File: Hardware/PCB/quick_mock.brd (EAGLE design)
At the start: 101.6 x 99.6 mm, 58 parts, among them Q3 600mA/40V

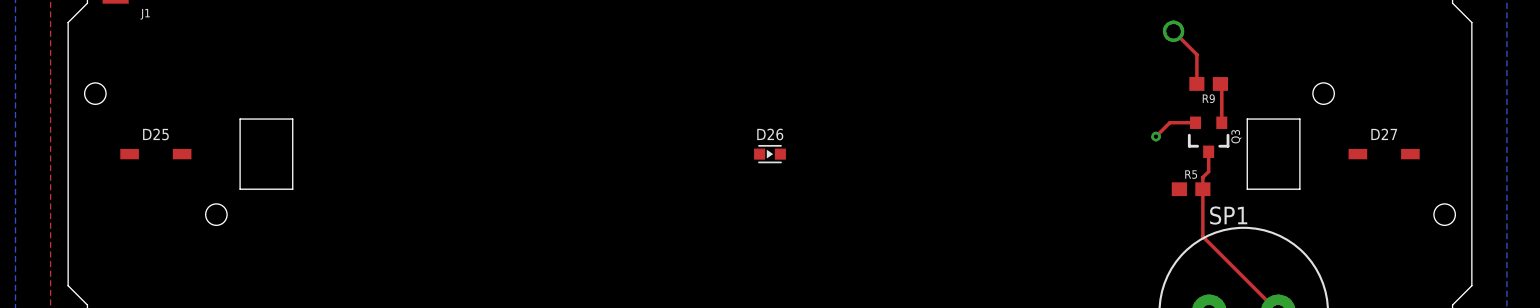
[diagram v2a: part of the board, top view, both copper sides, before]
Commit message: adjust LED placement. adjust hole and dimension placement.
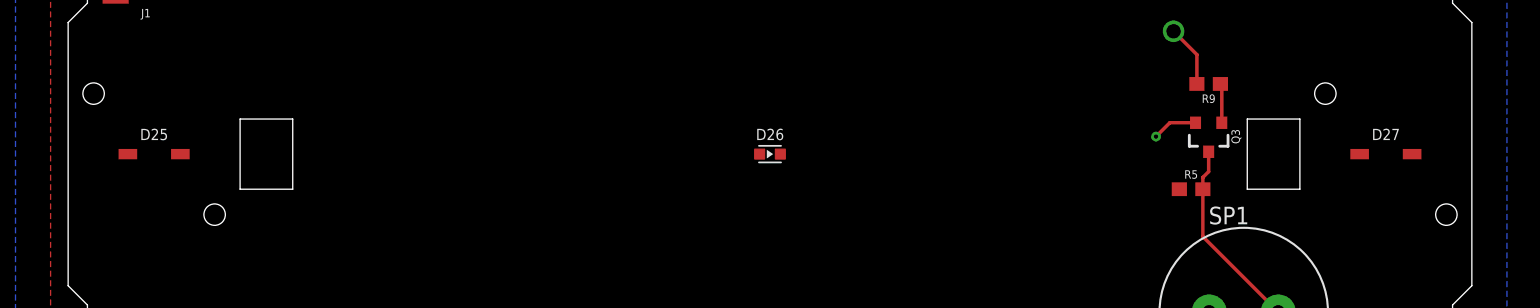
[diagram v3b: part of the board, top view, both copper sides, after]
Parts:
- moved D25 0.13 mm to (6.22, 50.8)
- moved D27 0.13 mm to (95.4, 50.8)
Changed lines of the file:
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@@
 <setting verticaltext="up"/>
 </settings>
-<grid distance="50" unitdist="mil" unit="inch" style="lines" multiple="1" display="yes" altdistance="5" altunitdist="mil" altunit="inch"/>
+<grid distance="50" unitdist="mil" unit="mm" style="lines" multiple="1" display="yes" altdistance="5" altunitdist="mil" altunit="inch"/>
 <layers>
 <layer number="1" name="Top" color="4" fill="1" visible="yes" active="yes"/>
@@
 <wire x1="13.446" y1="55.179990625" x2="13.446" y2="46.419990625" width="0.01" layer="200"/>
 <wire x1="88.17211875" y1="55.179990625" x2="88.17211875" y2="46.419990625" width="0.01" layer="200"/>
-<hole x="10.73" y="46.42" drill="1.55"/>
-<hole x="90.87" y="55.18" drill="1.55"/>
+<hole x="10.603" y="46.42" drill="1.55"/>
+<hole x="90.997" y="55.18" drill="1.55"/>
 <wire x1="90.87" y1="46.42" x2="99.63" y2="46.42" width="0.01" layer="201"/>
 <wire x1="99.63" y1="46.42" x2="99.63" y2="55.18" width="0.01" layer="201"/>
@@
 <wire x1="12.7" y1="0" x2="88.9" y2="0" width="0.01" layer="201"/>
 <wire x1="1.27" y1="88.9" x2="1.27" y2="12.7" width="0.01" layer="201"/>
-<wire x1="5.08" y1="50.8" x2="7.62" y2="50.8" width="0.1778" layer="51"/>
-<wire x1="6.35" y1="52.07" x2="6.35" y2="49.53" width="0.1778" layer="51"/>
-<wire x1="93.98" y1="50.8" x2="96.52" y2="50.8" width="0.1778" layer="51"/>
-<wire x1="95.25" y1="52.07" x2="95.25" y2="49.53" width="0.1778" layer="51"/>
+<wire x1="4.953" y1="50.8" x2="7.493" y2="50.8" width="0.1778" layer="51"/>
+<wire x1="6.223" y1="52.07" x2="6.223" y2="49.53" width="0.1778" layer="51"/>
+<wire x1="94.107" y1="50.8" x2="96.647" y2="50.8" width="0.1778" layer="51"/>
+<wire x1="95.377" y1="52.07" x2="95.377" y2="49.53" width="0.1778" layer="51"/>
 <wire x1="49.53" y1="50.8" x2="52.07" y2="50.8" width="0.1778" layer="51"/>
 <wire x1="50.8" y1="52.07" x2="50.8" y2="49.53" width="0.1778" layer="51"/>
@@
 <hole x="78.74" y="12.7" drill="2.794"/>
 <hole x="22.86" y="12.7" drill="2.794"/>
-<hole x="1.97" y="55.18" drill="1.55"/>
-<hole x="99.63" y="46.42" drill="1.55"/>
-<wire x1="7.62" y1="52.07" x2="11.43" y2="55.88" width="0.1778" layer="51"/>
-<text x="8.89" y="57.15" size="1.778" layer="51" font="vector">Transmitter</text>
+<hole x="1.843" y="55.18" drill="1.55"/>
+<hole x="99.757" y="46.42" drill="1.55"/>
+<wire x1="7.493" y1="52.07" x2="11.303" y2="55.88" width="0.1778" layer="51"/>
+<text x="8.763" y="57.15" size="1.778" layer="51" font="vector">Transmitter</text>
 <wire x1="52.07" y1="52.07" x2="55.88" y2="55.88" width="0.1778" layer="51"/>
 <text x="53.34" y="57.15" size="1.778" layer="51" font="vector">Receiver</text>
-<wire x1="96.52" y1="52.07" x2="100.33" y2="55.88" width="0.1778" layer="51"/>
-<text x="97.79" y="57.15" size="1.778" layer="51" font="vector">Transmitter</text>
+<wire x1="96.647" y1="52.07" x2="100.33" y2="55.88" width="0.1778" layer="51"/>
+<text x="97.917" y="57.15" size="1.778" layer="51" font="vector">Transmitter</text>
 <polygon width="0.1" layer="39">
 <vertex x="100.33" y="62.865"/>
@@
 <vertex x="99.06" y="37.846"/>
 </polygon>
-<circle x="99.63" y="46.42" radius="1.57" width="0" layer="39"/>
-<circle x="90.87" y="46.42" radius="1.57" width="0" layer="39"/>
-<circle x="99.63" y="55.18" radius="1.57" width="0" layer="39"/>
-<circle x="90.87" y="55.18" radius="1.57" width="0" layer="39"/>
-<circle x="10.73" y="46.42" radius="1.57" width="0" layer="39"/>
-<circle x="1.97" y="46.42" radius="1.57" width="0" layer="39"/>
-<circle x="10.73" y="55.18" radius="1.57" width="0" layer="39"/>
-<circle x="1.97" y="55.18" radius="1.57" width="0" layer="39"/>
+<circle x="99.757" y="46.42" radius="1.57" width="0" layer="39"/>
+<circle x="90.997" y="46.42" radius="1.57" width="0" layer="39"/>
+<circle x="99.757" y="55.18" radius="1.57" width="0" layer="39"/>
+<circle x="90.997" y="55.18" radius="1.57" width="0" layer="39"/>
+<circle x="10.603" y="46.42" radius="1.57" width="0" layer="39"/>
+<circle x="1.843" y="46.42" radius="1.57" width="0" layer="39"/>
+<circle x="10.603" y="55.18" radius="1.57" width="0" layer="39"/>
+<circle x="1.843" y="55.18" radius="1.57" width="0" layer="39"/>
 <polygon width="0.1" layer="39">
 <vertex x="50.8" y="71.882"/>
@@
 <attribute name="VALUE" x="8.6741" y="84.53628125" size="0.8128" layer="27" font="vector" ratio="12" align="top-center"/>
 </element>
-<element name="D25" library="Rob-Diodes" library_urn="urn:adsk.eagle:library:37150039" package="GULL-WING-2.3MM" package3d_urn="urn:adsk.eagle:package:39410737/2" value="VSMB2020X01" x="6.35" y="50.8" smashed="yes">
-<attribute name="NAME" x="6.35" y="51.816" size="0.8128" layer="25" font="vector" ratio="12" align="bottom-center"/>
-<attribute name="VALUE" x="6.35" y="49.784" size="0.8128" layer="27" font="vector" ratio="12" align="top-center"/>
+<element name="D25" library="Rob-Diodes" library_urn="urn:adsk.eagle:library:37150039" package="GULL-WING-2.3MM" package3d_urn="urn:adsk.eagle:package:39410737/2" value="VSMB2020X01" x="6.223" y="50.8" smashed="yes">
+<attribute name="NAME" x="6.223" y="51.816" size="0.8128" layer="25" font="vector" ratio="12" align="bottom-center"/>
+<attribute name="VALUE" x="6.223" y="49.784" size="0.8128" layer="27" font="vector" ratio="12" align="top-center"/>
 </element>
 <element name="D26" library="Rob-Diodes" library_urn="urn:adsk.eagle:library:37150039" package="SMD-603" package3d_urn="urn:adsk.eagle:package:37041000/3" value="LED-603" x="50.8" y="50.8" smashed="yes">
@@
 <attribute name="VALUE" x="50.8" y="49.784" size="0.8128" layer="27" font="vector" ratio="12" align="top-center"/>
 </element>
-<element name="D27" library="Rob-Diodes" library_urn="urn:adsk.eagle:library:37150039" package="GULL-WING-2.3MM" package3d_urn="urn:adsk.eagle:package:39410737/2" value="VSMB2020X01" x="95.25" y="50.8" smashed="yes">
-<attribute name="NAME" x="95.25" y="51.816" size="0.8128" layer="25" font="vector" ratio="12" align="bottom-center"/>
-<attribute name="VALUE" x="95.25" y="49.784" size="0.8128" layer="27" font="vector" ratio="12" align="top-center"/>
+<element name="D27" library="Rob-Diodes" library_urn="urn:adsk.eagle:library:37150039" package="GULL-WING-2.3MM" package3d_urn="urn:adsk.eagle:package:39410737/2" value="VSMB2020X01" x="95.377" y="50.8" smashed="yes">
+<attribute name="NAME" x="95.377" y="51.816" size="0.8128" layer="25" font="vector" ratio="12" align="bottom-center"/>
+<attribute name="VALUE" x="95.377" y="49.784" size="0.8128" layer="27" font="vector" ratio="12" align="top-center"/>
 </element>
 <element name="S2" library="IDEO-Switches" package="CUS-12_SPDT" override_package3d_urn="urn:adsk.eagle:package:39505090/2" override_package_urn="urn:adsk.eagle:footprint:39505091/1" value="CUS-12B" x="3.41" y="76.25" smashed="yes" rot="R270">

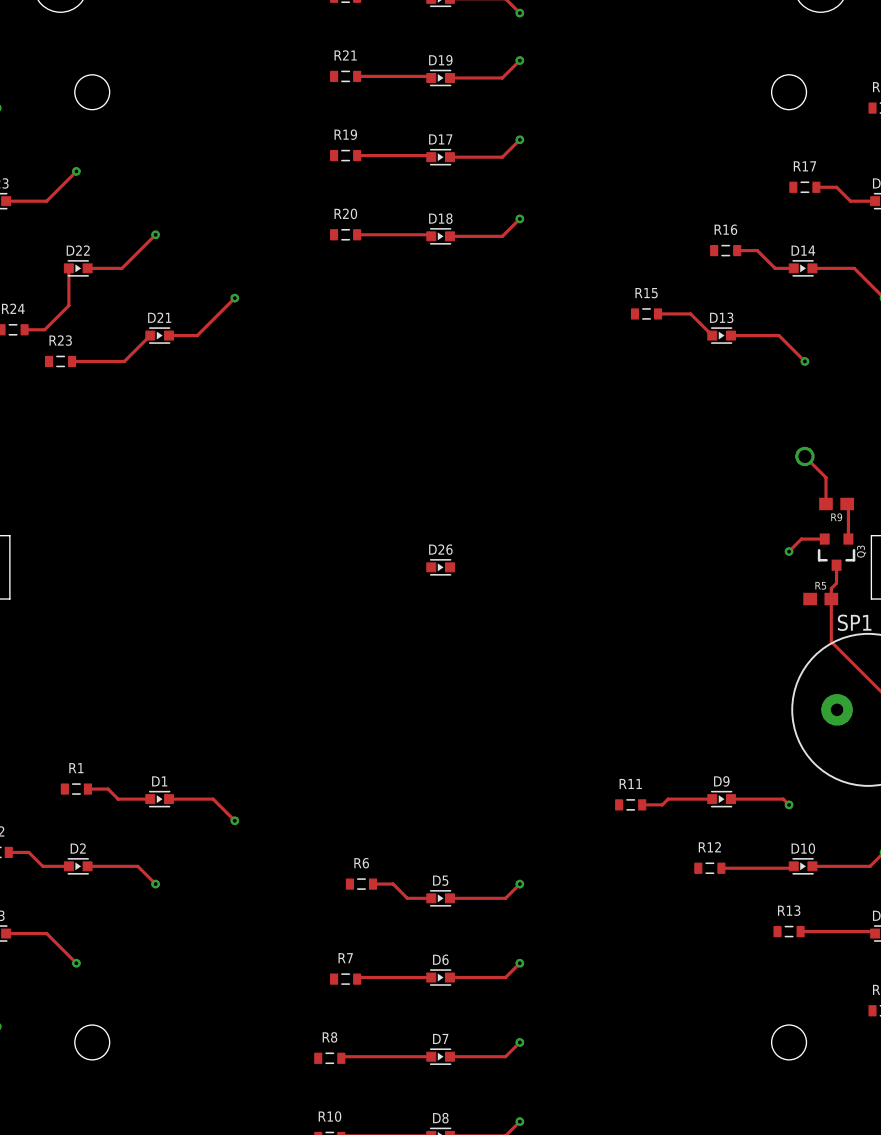
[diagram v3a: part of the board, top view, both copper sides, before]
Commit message: updates for new housing design
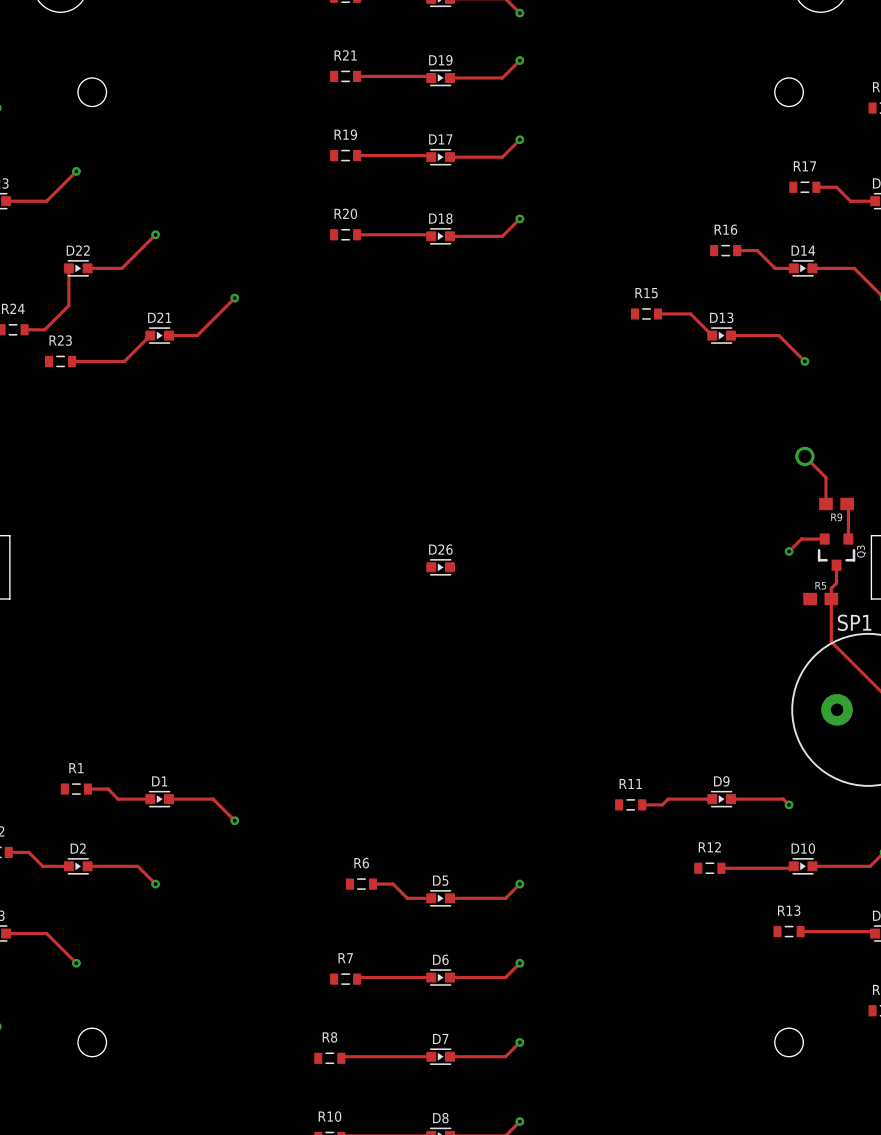
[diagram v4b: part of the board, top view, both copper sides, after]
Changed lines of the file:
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@@
 <setting verticaltext="up"/>
 </settings>
-<grid distance="50" unitdist="mil" unit="mm" style="lines" multiple="1" display="yes" altdistance="5" altunitdist="mil" altunit="inch"/>
+<grid distance="50" unitdist="mil" unit="inch" style="lines" multiple="1" display="yes" altdistance="5" altunitdist="mil" altunit="inch"/>
 <layers>
 <layer number="1" name="Top" color="4" fill="1" visible="yes" active="yes"/>
@@
 <wire x1="0" y1="41.275" x2="0" y2="60.325" width="0.0254" layer="20"/>
 <wire x1="0" y1="60.325" x2="1.397" y2="61.722" width="0.0254" layer="20"/>
-<hole x="22.86" y="88.9" drill="2.794"/>
-<hole x="78.74" y="88.9" drill="2.794"/>
-<hole x="78.74" y="12.7" drill="2.794"/>
-<hole x="22.86" y="12.7" drill="2.794"/>
+<hole x="22.86" y="88.9" drill="2.286"/>
+<hole x="78.74" y="88.9" drill="2.286"/>
+<hole x="78.74" y="12.7" drill="2.286"/>
+<hole x="22.86" y="12.7" drill="2.286"/>
 <hole x="1.843" y="55.18" drill="1.55"/>
 <hole x="99.757" y="46.42" drill="1.55"/>
